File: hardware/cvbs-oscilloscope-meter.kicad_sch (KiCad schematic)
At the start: 42 parts, among them J1 Conn_Coaxial_Power, J2 Conn_Coaxial_Power, J3 Conn_Coaxial_Power, J4 Conn_Coaxial_Power, Q1 2N3906, Q2 2N3906, Q3 2N3904, Q4 2N3904, Q5 2N3904, Q6 2N3904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

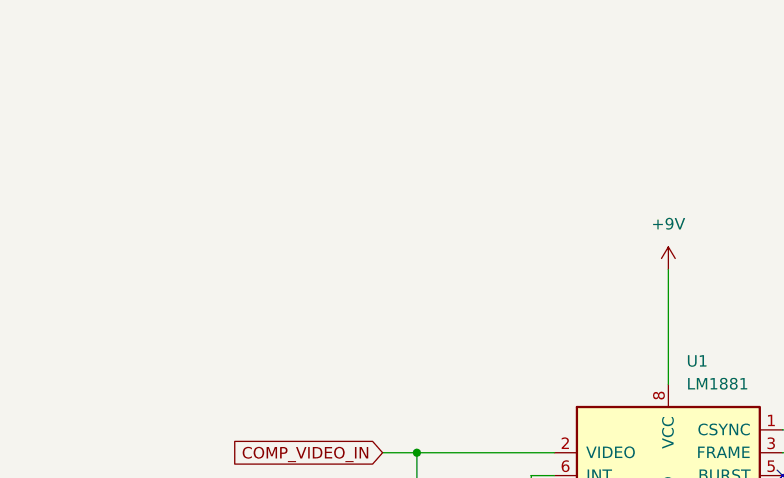
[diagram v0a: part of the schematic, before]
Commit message: New update
- Updated README
- Added power and LED circuitry
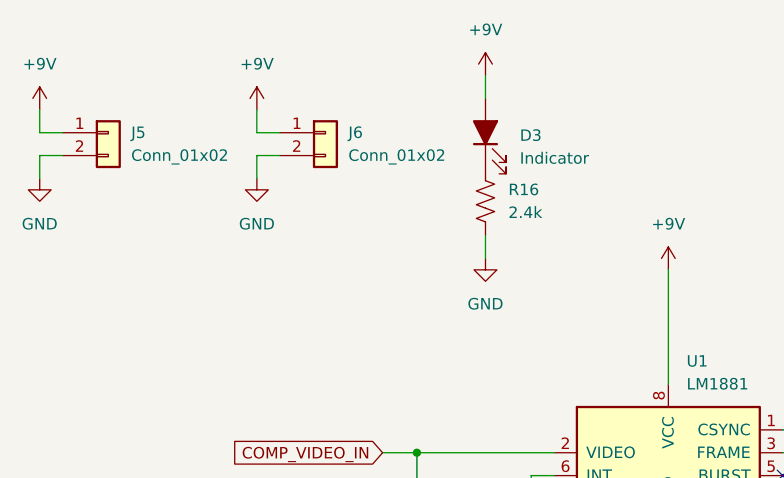
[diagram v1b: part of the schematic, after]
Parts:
- added D3: Indicator, LED_THT:LED_D5.0mm, symbol Device:LED_Filled
- added J5: Conn_01x02, Connector_Molex:Molex_KK-396_A-41791-0002_1x02_P3.96mm_Vertical, symbol Connector_Generic:Conn_01x02
- added J6: Conn_01x02, Connector_BarrelJack:BarrelJack_CUI_PJ-063AH_Horizontal, symbol Connector_Generic:Conn_01x02
- added R16: 2.4k, Resistor_THT:R_Axial_DIN0207_L6.3mm_D2.5mm_P10.16mm_Horizontal, symbol Device:R_US
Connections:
- net +9V: now also D3.2 (A), J5.1 (Pin_1), J6.1 (Pin_1)
- net GND: now also J5.2 (Pin_2), J6.2 (Pin_2), R16.2
- new net: D3.1 (K), R16.1
